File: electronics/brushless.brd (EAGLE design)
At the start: 35.5 x 43.3 mm, 69 parts, among them J1 USB_MINI-B_SMT, Q1 BUK7Y12-40E, Q2 BUK7Y12-40E, Q3 BUK7Y12-40E, Q4 BUK7Y12-40E, Q5 BUK7Y12-40E, Q6 BUK7Y12-40E, X1 JST-XH-10-PIN-LONG-PAD

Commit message: Controller board
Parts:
- added U$6: (no value), rhoban:E3,5-8
- moved R50 22.8 mm to (14.8, 9.10)
- moved R13 21.1 mm to (14.0, 9.70), turned to 180 degrees
- moved D4 20.9 mm to (17.5, 12.8), turned to 0 degrees
- moved R28 20.0 mm to (16.9, 8.97)
- moved U$4 18.3 mm to (6.01, 10.8), flipped to the top, turned to 270 degrees
- moved R36 18.1 mm to (14.0, 13.6), turned to 270 degrees
- moved R29 17.0 mm to (19.6, 8.06), turned to 180 degrees
- moved R35 16.2 mm to (19.6, 9.97), turned to 180 degrees
- moved Q6 14.2 mm to (17.6, 39.2)
- moved Q5 13.9 mm to (18.2, 27.1)
- moved R21 13.1 mm to (28.6, 10.9), turned to 270 degrees
- moved Q3 13.1 mm to (10.1, 27.1)
- moved Q4 13.1 mm to (10.1, 39.2)
- moved R19 12.5 mm to (17.5, 42.7), turned to 90 degrees
- moved R6 12.5 mm to (19.4, 42.7), turned to 270 degrees
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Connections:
- net ENC_B: now also X1.5; no longer X1.4
- net GND: now also U$6.-
- net HALLV: now also X1.9; no longer X1.7
- net V+: now also U$6.+
- net V_PHASE: now also X1.4; no longer X1.5
- net W_PHASE: now also X1.7; no longer X1.9
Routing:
- net V+: track 15.3 -> 25.9 mm
- net V_PHASE: track 11.5 -> 14.4 mm
- net U_PHASE: track 14.4 -> 12.2 mm
- net GND: track 47.9 -> 49.4 mm
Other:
- board size 35.5 x 43.3 mm -> 30.1 x 46.1 mm
- board text added: "REV0"
- board text added: "RHOBAN BLDC"

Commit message: Small tweaks
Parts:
- moved C20 13.0 mm to (11.5, 28.1), turned to 270 degrees
- moved C21 12.2 mm to (19.1, 28.1), turned to 90 degrees
- moved OSC 10.1 mm to (15.3, 28.1), turned to 0 degrees
- moved UC1 4.64 mm to (16.2, 20.9), turned to 180 degrees
- moved J1 0.40 mm to (25.1, 9.53)
- moved U$5 0.25 mm to (9.37, 5.04)
- moved R29 0.13 mm to (19.5, 8.06)
- moved R35 0.13 mm to (19.5, 9.97)
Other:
- board size 30.1 x 46.1 mm -> 30 x 46 mm

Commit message: Farnell refs & names
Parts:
- removed U$1, U$2, U$3: OPEN-BLDC_IR2101, rhoban:OPEN-BLDC_SO-8
- removed U$4: TS2940CW-3.3RP, rhoban:SOT223
- removed U$5: CONNEC_1X08, rhoban:CONNEC_1X08
- added DRV1, DRV2, DRV3: OPEN-BLDC_IR2101, rhoban:OPEN-BLDC_SO-8
- added LOGIC: CONNEC_1X08, rhoban:CONNEC_1X08
- added REG1: TS2940CW-3.3RP, rhoban:SOT223
- C4: value 1nF -> 1000pF
- U$6: value (none) -> 100uF
- moved U$6 3.30 mm to (24.8, 38.2)
- moved Q1 3.30 mm to (3.54, 23.8)
- moved Q3 3.30 mm to (10.1, 23.8)
- moved Q5 3.30 mm to (18.2, 23.8)
- moved R23 3.30 mm to (22.9, 26.0)
- moved R24 3.30 mm to (26.7, 26.1)
- moved R48 3.30 mm to (24.4, 22.3)
- moved C7 3.30 mm to (8.99, 14.1)
- moved D1 3.30 mm to (9.31, 14.4)
- moved D2 3.30 mm to (18.2, 14.4)
- moved R40 3.30 mm to (24.4, 15.9)
- moved RESET 3.30 mm to (27.7, 14.9)
- moved J1 3.30 mm to (25.1, 6.23)
- moved R21 3.30 mm to (28.6, 7.62)
- moved R28 3.30 mm to (16.9, 5.67)
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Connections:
- net 3.3: now also LOGIC.3, REG1.3; no longer U$4.3, U$5.3
- net CS: now also LOGIC.5; no longer U$5.5
- net GND: now also DRV1.4, DRV2.4, DRV3.4, LOGIC.1, REG1.2; no longer U$1.4, U$2.4, U$3.4, U$4.2, U$5.1
- net MISO: now also LOGIC.8; no longer U$5.8
- net MOSI: now also LOGIC.7; no longer U$5.7
- net N$10: now also DRV2.8; no longer U$2.8
- net N$11: now also DRV1.6; no longer U$1.6
- net N$12: now also DRV2.2; no longer U$2.2
- net N$13: now also DRV2.3; no longer U$2.3
- net N$14: now also DRV2.6; no longer U$2.6
- net N$15: now also DRV3.8; no longer U$3.8
- net N$16: now also DRV3.2; no longer U$3.2
- net N$17: now also DRV3.3; no longer U$3.3
- net N$18: now also DRV3.6; no longer U$3.6
- net N$4: now also DRV1.2; no longer U$1.2
- net N$5: now also DRV1.8; no longer U$1.8
- net N$8: now also DRV1.3; no longer U$1.3
- net SCK: now also LOGIC.6; no longer U$5.6
- net U_GATE_HIGH: now also DRV1.7; no longer U$1.7
- net U_GATE_LOW: now also DRV1.5; no longer U$1.5
- net VCC: now also LOGIC.2, REG1.1; no longer U$4.1, U$5.2
- net VDRIVER: now also DRV1.1, DRV2.1, DRV3.1, LOGIC.4; no longer U$1.1, U$2.1, U$3.1, U$5.4
- net V_GATE_HIGH: now also DRV2.7; no longer U$2.7
- net V_GATE_LOW: now also DRV2.5; no longer U$2.5
- net W_GATE_HIGH: now also DRV3.7; no longer U$3.7
- net W_GATE_LOW: now also DRV3.5; no longer U$3.5
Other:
- board text added: ""MAY THE FORCE"
- board text added: "--------------------------"
- board text added: "BE WITH US""
- board text added: "RHOBAN BLDC REV0"
- board text removed: "REV0"
- board text removed: "RHOBAN BLDC"

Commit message: bstop
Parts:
- renumbered U$6 to C10, U$7 to SENSE
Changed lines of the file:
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@@
 <text x="12.192" y="43.561" size="0.8128" layer="25">BE WITH US"</text>
 <text x="9.906" y="42.926" size="0.8128" layer="25">--------------------------</text>
+<wire x1="2.921" y1="44.196" x2="2.921" y2="40.64" width="1.9304" layer="30"/>
+<wire x1="2.921" y1="40.64" x2="2.921" y2="38.608" width="1.9304" layer="30"/>
+<wire x1="1.905" y1="38.735" x2="3.81" y2="38.735" width="1.9304" layer="30"/>
+<wire x1="3.81" y1="38.735" x2="3.81" y2="38.608" width="1.9304" layer="30"/>
+<wire x1="5.461" y1="44.323" x2="5.461" y2="40.64" width="1.9304" layer="30"/>
+<wire x1="8.001" y1="44.323" x2="7.874" y2="44.323" width="1.9304" layer="30"/>
+<wire x1="7.874" y1="44.323" x2="7.874" y2="40.64" width="1.9304" layer="30"/>
+<wire x1="2.921" y1="40.64" x2="8.89" y2="40.64" width="1.9304" layer="30"/>
+<wire x1="8.89" y1="40.64" x2="20.574" y2="40.64" width="1.9304" layer="30"/>
+<wire x1="20.574" y1="40.64" x2="22.987" y2="38.227" width="1.9304" layer="30"/>
+<wire x1="8.001" y1="38.481" x2="8.89" y2="38.481" width="1.9304" layer="30"/>
+<wire x1="8.89" y1="38.481" x2="10.287" y2="38.481" width="1.9304" layer="30"/>
+<wire x1="10.287" y1="38.481" x2="10.414" y2="38.608" width="1.9304" layer="30"/>
+<wire x1="15.621" y1="38.608" x2="17.907" y2="38.608" width="1.9304" layer="30"/>
+<wire x1="17.907" y1="38.608" x2="17.907" y2="38.481" width="1.9304" layer="30"/>
+<wire x1="16.383" y1="40.513" x2="16.383" y2="38.862" width="1.9304" layer="30"/>
+<wire x1="8.89" y1="38.481" x2="8.89" y2="40.64" width="1.9304" layer="30"/>
+<wire x1="2.413" y1="33.401" x2="2.413" y2="26.543" width="1.9304" layer="30"/>
+<wire x1="10.033" y1="33.528" x2="10.033" y2="26.67" width="1.9304" layer="30"/>
+<wire x1="17.653" y1="33.401" x2="17.653" y2="26.543" width="1.9304" layer="30"/>
+<wire x1="1.397" y1="26.416" x2="3.683" y2="26.416" width="1.9304" layer="30"/>
+<wire x1="3.683" y1="26.416" x2="3.81" y2="26.543" width="1.9304" layer="30"/>
+<wire x1="8.255" y1="26.416" x2="10.414" y2="26.416" width="1.9304" layer="30"/>
+<wire x1="16.383" y1="26.543" x2="18.415" y2="26.543" width="1.9304" layer="30"/>
+<wire x1="18.415" y1="26.543" x2="18.542" y2="26.416" width="1.9304" layer="30"/>
+<wire x1="3.556" y1="22.86" x2="22.098" y2="22.86" width="1.9304" layer="30"/>
+<wire x1="22.098" y1="22.733" x2="22.098" y2="26.289" width="1.9304" layer="30"/>
+<wire x1="22.098" y1="26.289" x2="24.765" y2="26.289" width="1.9304" layer="30"/>
+<wire x1="26.924" y1="26.289" x2="27.813" y2="26.289" width="1.9304" layer="30"/>
+<wire x1="27.813" y1="26.289" x2="27.813" y2="26.416" width="1.9304" layer="30"/>
+<wire x1="27.813" y1="26.416" x2="27.686" y2="26.416" width="1.9304" layer="30"/>
+<wire x1="27.686" y1="26.416" x2="27.686" y2="38.354" width="1.9304" layer="30"/>
+<wire x1="27.686" y1="38.354" x2="27.559" y2="44.069" width="1.9304" layer="30"/>
+<wire x1="27.559" y1="44.069" x2="21.844" y2="44.069" width="1.9304" layer="30"/>
 </plain>
 <attributes>
@@
 <attribute name="FARNELL" value="1842013" x="5.2164" y="16.7688" size="1.778" layer="27" display="off"/>
 </element>
-<element name="U$7" library="rhoban" package="SO8" value="ACS712" x="25.835" y="23.81" rot="MR270">
+<element name="SENSE" library="rhoban" package="SO8" value="ACS712" x="25.835" y="23.81" rot="MR270">
 <attribute name="FARNELL" value="1329624" x="25.835" y="23.81" size="1.778" layer="28" rot="MR270" display="off"/>
 </element>
@@
 <attribute name="FARNELL" value="2446965" x="28.575" y="7.62" size="1.778" layer="28" rot="MR270" display="off"/>
 </element>
-<element name="U$6" library="rhoban" package="E3,5-8" value="100uF" x="24.765" y="38.227" rot="R180">
+<element name="C10" library="rhoban" package="E3,5-8" value="100uF" x="24.765" y="38.227" rot="R180">
 <attribute name="FARNELL" value="1144713" x="24.765" y="38.227" size="1.778" layer="27" rot="R180" display="off"/>
 </element>
@@
 <wire x1="8.16" y1="40.6448" x2="5.52" y2="40.6448" width="1.778" layer="16"/>
 <wire x1="5.52" y1="40.6448" x2="2.905" y2="40.6448" width="1.778" layer="16"/>
-<contactref element="U$7" pad="5"/>
+<contactref element="SENSE" pad="5"/>
 <contactref element="C4" pad="2"/>
 <contactref element="R21" pad="2"/>
@@
 <wire x1="8.16" y1="38.545" x2="8.92" y2="38.545" width="1.6764" layer="16"/>
 <wire x1="8.92" y1="38.545" x2="8.92" y2="40.73" width="1.6764" layer="16"/>
-<contactref element="U$6" pad="-"/>
+<contactref element="C10" pad="-"/>
 <wire x1="22.987" y1="38.227" x2="20.574" y2="40.767" width="1.6764" layer="16"/>
 <wire x1="20.574" y1="40.767" x2="15.367" y2="40.767" width="1.6764" layer="16"/>
@@
 <contactref element="V+" pad="2"/>
 <contactref element="V+" pad="1"/>
-<contactref element="U$7" pad="4"/>
-<contactref element="U$7" pad="3"/>
-<contactref element="U$6" pad="+"/>
+<contactref element="SENSE" pad="4"/>
+<contactref element="SENSE" pad="3"/>
+<contactref element="C10" pad="+"/>
 <wire x1="24.47" y1="44.093" x2="21.93" y2="44.093" width="2" layer="16"/>
 <wire x1="27.74" y1="26.2738" x2="27.74" y2="38.481" width="2" layer="16"/>
@@
 <contactref element="REG1" pad="1"/>
 <contactref element="X1" pad="2"/>
-<contactref element="U$7" pad="8"/>
+<contactref element="SENSE" pad="8"/>
 <wire x1="16.9932" y1="1.7412" x2="23.93" y2="21.3462" width="0" layer="19" extent="16-16"/>
 <wire x1="2.9082" y1="9.812" x2="16.9932" y2="1.7412" width="0" layer="19" extent="1-1"/>
@@
 <wire x1="3.54" y1="22.83" x2="10.065" y2="22.83" width="1.778" layer="16"/>
 <wire x1="10.065" y1="22.83" x2="18.19" y2="22.83" width="1.778" layer="16"/>
-<contactref element="U$7" pad="2"/>
-<contactref element="U$7" pad="1"/>
+<contactref element="SENSE" pad="2"/>
+<contactref element="SENSE" pad="1"/>
 <wire x1="23.93" y1="26.2738" x2="25.2" y2="26.2738" width="1.2" layer="16"/>
 <wire x1="23.93" y1="26.2738" x2="22.12" y2="26.2738" width="1.6764" layer="16"/>
@@
 </signal>
 <signal name="N$24">
-<contactref element="U$7" pad="7"/>
+<contactref element="SENSE" pad="7"/>
 <contactref element="R20" pad="1"/>
 <wire x1="28.575" y1="11.822" x2="25.2" y2="21.3462" width="0" layer="19" extent="16-16"/>
 </signal>
 <signal name="N$27">
-<contactref element="U$7" pad="6"/>
+<contactref element="SENSE" pad="6"/>
 <contactref element="C4" pad="1"/>
 <wire x1="28.72" y1="17.415" x2="26.47" y2="21.3462" width="0" layer="19" extent="16-16"/>

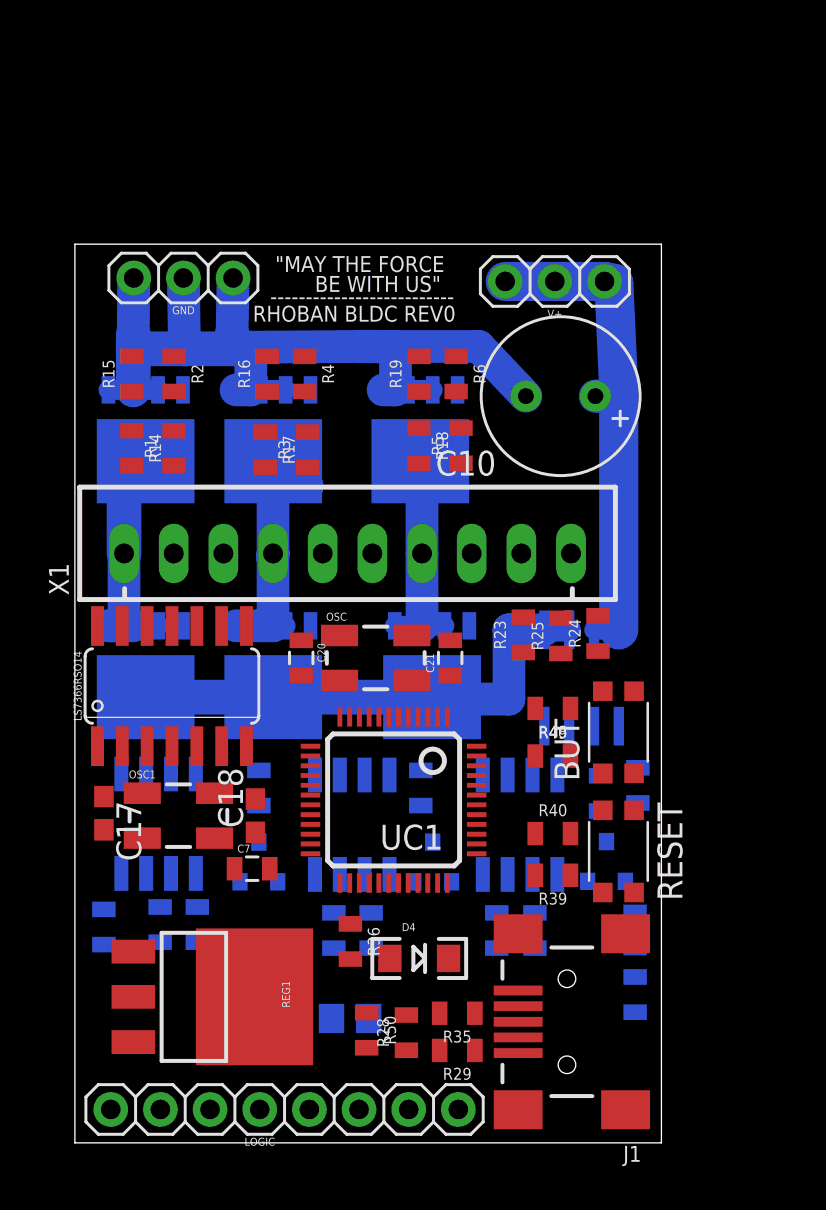
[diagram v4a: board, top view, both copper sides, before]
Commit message: Moving to vertical micro usb connector, adding silk
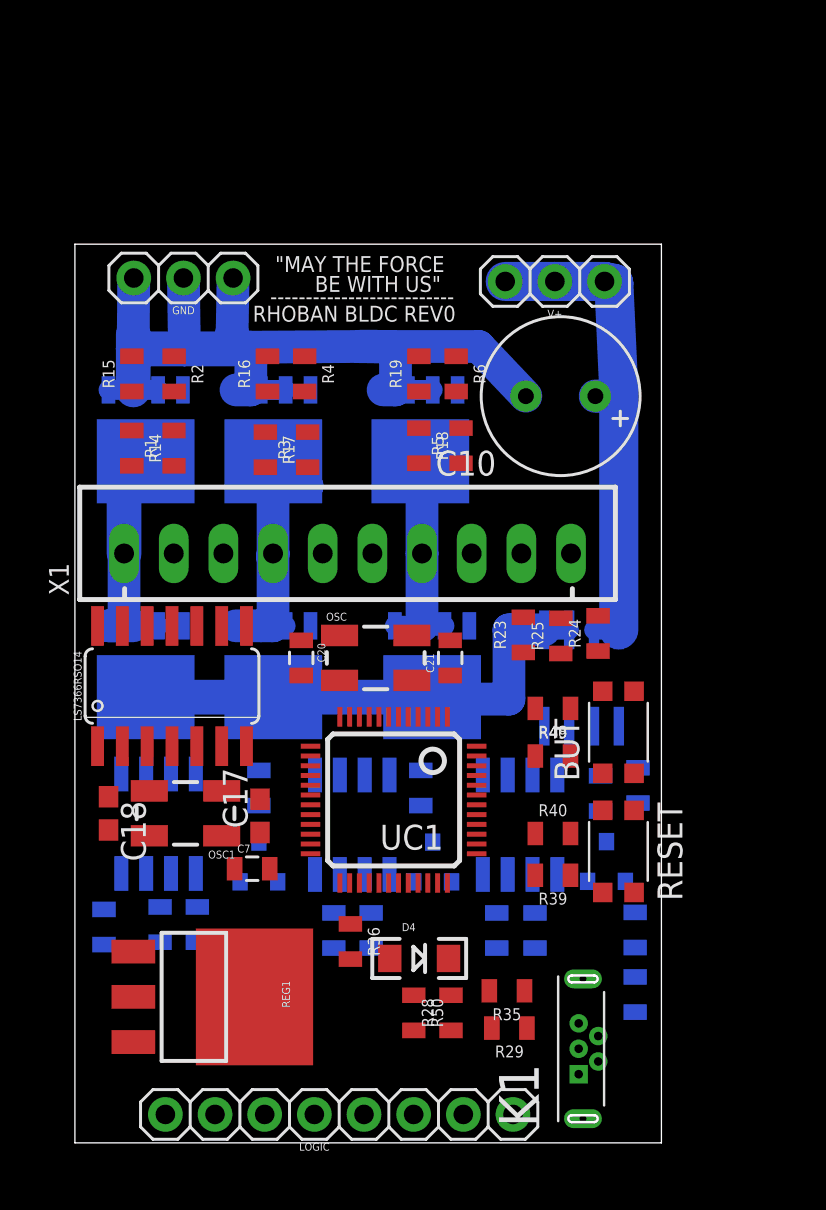
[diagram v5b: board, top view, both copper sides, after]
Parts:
- removed J1: USB_MINI-B_SMT, SparkFun-Connectors:USB-MINIB
- added K1: (no value), Wurth_Input-Output_Connectors_rev15d:614105150721
- moved C17 7.98 mm to (9.39, 16.8), turned to 90 degrees
- moved C18 7.51 mm to (1.64, 16.9), turned to 270 degrees
- moved R13 5.15 mm to (9.04, 7.79)
- moved R29 2.90 mm to (22.1, 5.90)
- moved LOGIC 2.81 mm to (12.2, 1.49)
- moved R35 2.79 mm to (22.0, 7.81)
- moved R50 2.57 mm to (17.3, 6.68)
- moved R28 2.50 mm to (19.2, 6.68)
- moved OSC1 0.38 mm to (5.58, 16.9), turned to 180 degrees
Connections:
- net GND: now also K1.5, K1.Z1, K1.Z2; no longer J1.GND, J1.S1, J1.S2, J1.S3, J1.S4
- net N$59: now also K1.2; no longer J1.D-
- net N$60: now also K1.3; no longer J1.D+
- net VUSB: now also K1.1; no longer J1.VBUS
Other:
- board text added: "3.3"
- board text added: "CS"
- board text added: "GND"
- board text added: "MISO"
- board text added: "MOSI"
- board text added: "SCK"
- board text added: "V+"
- board text added: "VCC"
- board text added: "VDRIVER"

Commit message: Brushless board
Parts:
- removed R13: 0Ohm, rhoban:R0805
- added D5: (no value), SparkFun-DiscreteSemi:SOD-323
- added JP1, JP2: JUMPER-SMT_2_NO_NO-SILK_ROUND, SparkFun-Jumpers:SMT-JUMPER_2_NO_NO-SILK_ROUND
- moved REG1 0.46 mm to (5.63, 7.25)
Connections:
- new net N$22: JP2.2, REG1.1
- net V+: now also JP1.1; no longer R13.1
- net VCC: now also D5.1, JP2.1; no longer REG1.1
- net VDRIVER: now also JP1.2; no longer R13.2
- net VUSB: now also D5.2
